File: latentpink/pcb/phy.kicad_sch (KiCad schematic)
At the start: 0 parts

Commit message: Continued initial schematic capture and floorplanning
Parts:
- added U1: VSC8512, azonenberg_pcb:BGA_672_27x27_DEPOPCORNER_1MM, symbol microchip-azonenberg:VSC8512
- added U2: XC7K160T-2FBG484C, azonenberg_pcb:BGA_484_22x22_FULLARRAY_1MM, symbol xilinx-azonenberg:XC7KxT-FBG484
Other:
- added sheet QSGMII Power (qsgmii-power.kicad_sch)
- company: (none) -> Antikernel Labs

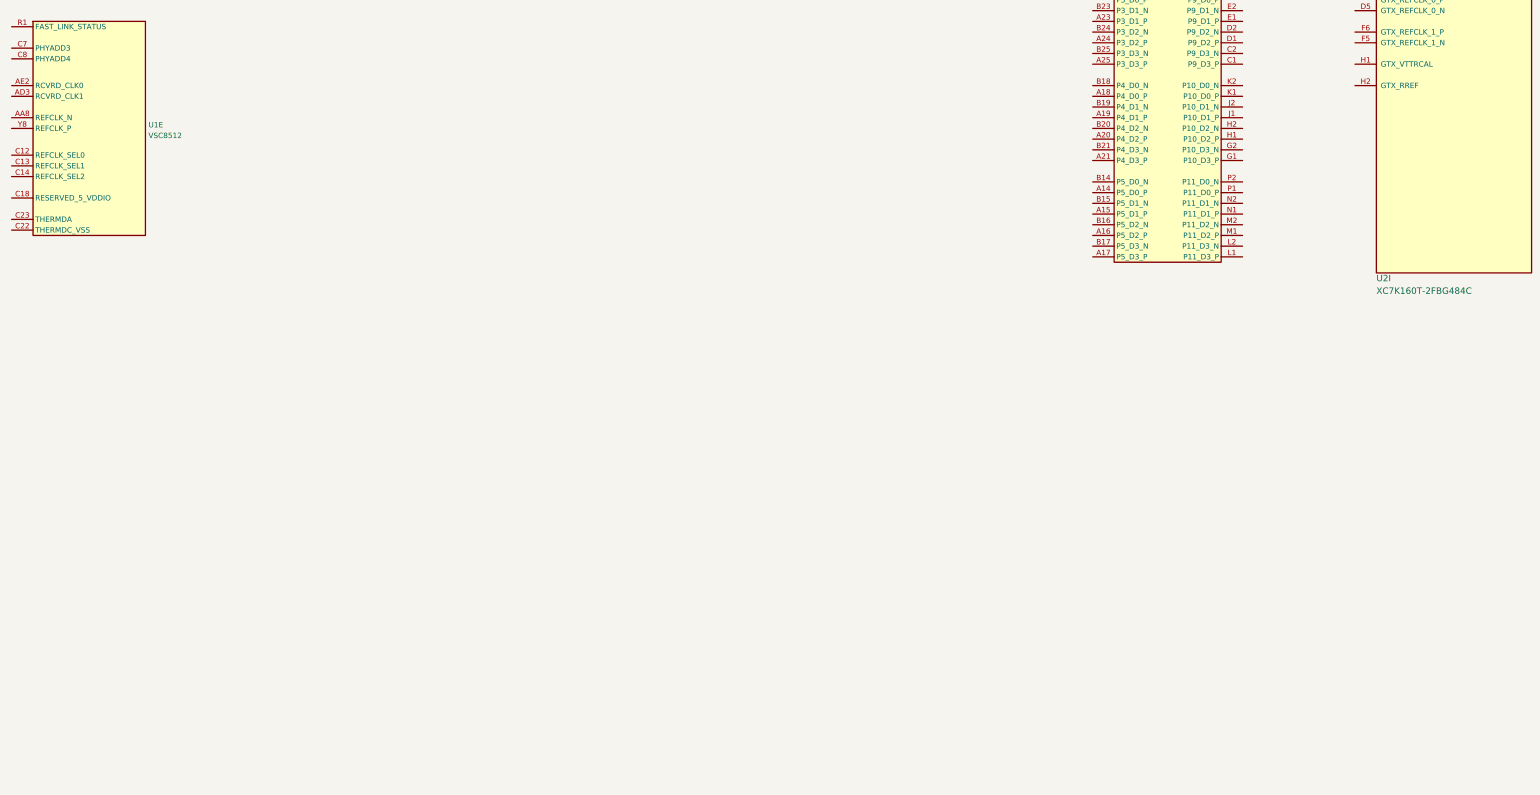
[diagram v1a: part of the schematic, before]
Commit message: Continued initial schematic capture
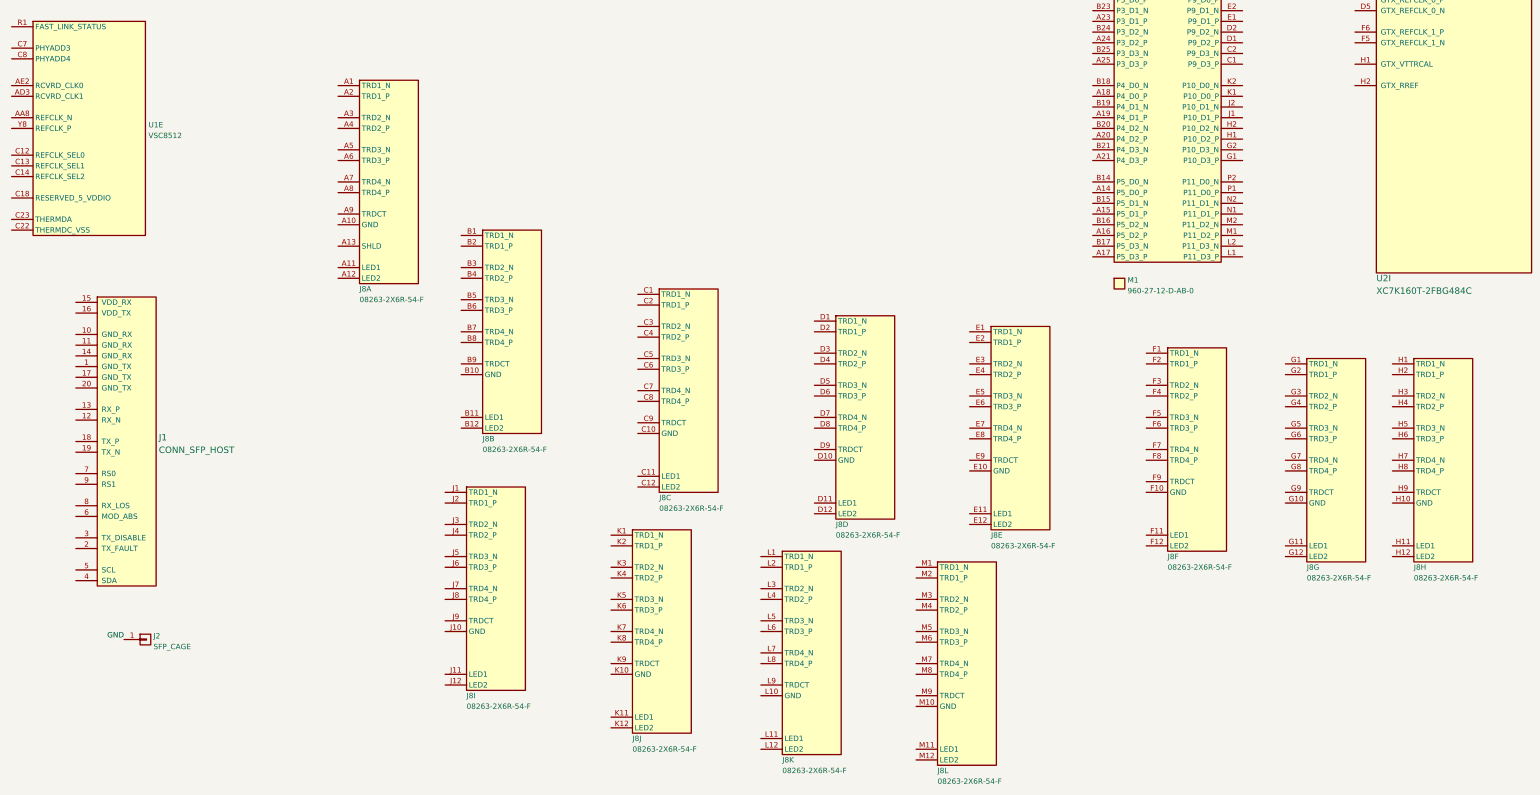
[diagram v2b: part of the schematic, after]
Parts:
- added J1: CONN_SFP_HOST, azonenberg_pcb:CONN_SFP+_AMPHENOL_UE76_A10_2000T, symbol special-azonenberg:CONN_SFP_HOST
- added J2: SFP_CAGE, azonenberg_pcb:CONN_SFP_CAGE_TE_2007194-1, symbol conn:CONN_01X01
- added J8: 08263-2X6R-54-F, azonenberg_pcb:CONN_RJ45_BELFUSE_0863-2X6R-54-F, symbol special-azonenberg:BEL_FUSE_08263-2X6R-54-F
- added M1: 960-27-12-D-AB-0, azonenberg_pcb:HEATSINK_WAKEFIELDVETTE_960-27-12-D-AB-0, symbol special-azonenberg:MECHANICAL
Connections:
- new net GND: J2.1 (P1)

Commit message: Continued work on QSGMII subsystem
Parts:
- added C334, C335, C336, C337, C338, C339, C340, C341, C342, C343, C346, C347, C348, C349, C350, C351: 0.1 uF, azonenberg_pcb:EIA_0402_CAP_NOSILK, symbol device:C
- added C344, C345: 0.47 uF, azonenberg_pcb:EIA_0402_CAP_NOSILK, symbol device:C
- added R78, R79: 4.7K, azonenberg_pcb:EIA_0402_RES_NOSILK, symbol device:R
- added R80: 100, symbol device:R
- added U24, U25: OSC_LVDS, symbol osc-azonenberg:OSC_LVDS
- added U4: STM32H735-UFBGA176-25, azonenberg_pcb:BGA_201_10x10_DEPOP_0.65MM_OSHPARK, symbol st-azonenberg:STM32H735-UFBGA176-25
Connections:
- net GND: now also J1.1 (GND_TX), J1.10 (GND_RX), J1.11 (GND_RX), J1.14 (GND_RX), J1.17 (GND_TX), J1.20 (GND_TX), J8.A10 (GND), J8.B10 (GND), J8.C10 (GND), J8.D10 (GND), J8.E10 (GND), J8.F10 (GND), J8.G10 (GND), J8.H10 (GND), J8.J10 (GND), J8.K10 (GND), J8.L10 (GND), J8.M10 (GND)
- net ETH6_D0_P: now reaches U1.A10 (P6_D0_P)
- net ETH6_D0_P: now also J8.G2 (TRD1_P)
- net ETH6_D1_P: now reaches U1.A11 (P6_D1_P)
- net ETH6_D1_P: now also J8.G4 (TRD2_P)
- net ETH6_D2_P: now reaches U1.A12 (P6_D2_P)
- net ETH6_D2_P: now also J8.G6 (TRD3_P)
- net ETH6_D3_P: now reaches U1.A13 (P6_D3_P)
- net ETH6_D3_P: now also J8.G8 (TRD4_P)
- net ETH5_D0_P: now reaches U1.A14 (P5_D0_P)
- net ETH5_D0_P: now also J8.F2 (TRD1_P)
- net ETH5_D1_P: now reaches U1.A15 (P5_D1_P)
- net ETH5_D1_P: now also J8.F4 (TRD2_P)
- net ETH5_D2_P: now reaches U1.A16 (P5_D2_P)
- net ETH5_D2_P: now also J8.F6 (TRD3_P)
- net ETH5_D3_P: now reaches U1.A17 (P5_D3_P)
- net ETH5_D3_P: now also J8.F8 (TRD4_P)
- net ETH4_D0_P: now reaches U1.A18 (P4_D0_P)
- net ETH4_D0_P: now also J8.E2 (TRD1_P)
- net ETH4_D1_P: now reaches U1.A19 (P4_D1_P)
- net ETH4_D1_P: now also J8.E4 (TRD2_P)
- net ETH8_D0_P: now reaches U1.A2 (P8_D0_P)
- net ETH8_D0_P: now also J8.J2 (TRD1_P)
- net ETH4_D2_P: now reaches U1.A20 (P4_D2_P)
- net ETH4_D2_P: now also J8.E6 (TRD3_P)
- net ETH4_D3_P: now reaches U1.A21 (P4_D3_P)
- net ETH4_D3_P: now also J8.E8 (TRD4_P)
- net ETH3_D0_P: now reaches U1.A22 (P3_D0_P)
- net ETH3_D0_P: now also J8.D2 (TRD1_P)
- net ETH3_D1_P: now reaches U1.A23 (P3_D1_P)
- net ETH3_D1_P: now also J8.D4 (TRD2_P)
- net ETH3_D2_P: now reaches U1.A24 (P3_D2_P)
- net ETH3_D2_P: now also J8.D6 (TRD3_P)
- net ETH3_D3_P: now reaches U1.A25 (P3_D3_P)
- net ETH3_D3_P: now also J8.D8 (TRD4_P)
- net ETH8_D1_P: now reaches U1.A3 (P8_D1_P)
- net ETH8_D1_P: now also J8.J4 (TRD2_P)
- net ETH8_D2_P: now reaches U1.A4 (P8_D2_P)
- net ETH8_D2_P: now also J8.J6 (TRD3_P)
- net ETH8_D3_P: now reaches U1.A5 (P8_D3_P)
- net ETH8_D3_P: now also J8.J8 (TRD4_P)
- net ETH7_D0_P: now reaches U1.A6 (P7_D0_P)
- net ETH7_D0_P: now also J8.H2 (TRD1_P)
- net ETH7_D1_P: now reaches U1.A7 (P7_D1_P)
- net ETH7_D1_P: now also J8.H4 (TRD2_P)
- net ETH7_D2_P: now reaches U1.A8 (P7_D2_P)
- net ETH7_D2_P: now also J8.H6 (TRD3_P)
- net ETH7_D3_P: now reaches U1.A9 (P7_D3_P)
- net ETH7_D3_P: now also J8.H8 (TRD4_P)
- net ETH6_D0_N: now reaches U1.B10 (P6_D0_N)
- net ETH6_D0_N: now also J8.G1 (TRD1_N)
- net ETH6_D1_N: now reaches U1.B11 (P6_D1_N)
- net ETH6_D1_N: now also J8.G3 (TRD2_N)
- net ETH6_D2_N: now reaches U1.B12 (P6_D2_N)
- net ETH6_D2_N: now also J8.G5 (TRD3_N)
- net ETH6_D3_N: now reaches U1.B13 (P6_D3_N)
- net ETH6_D3_N: now also J8.G7 (TRD4_N)
- net ETH5_D0_N: now reaches U1.B14 (P5_D0_N)
- net ETH5_D0_N: now also J8.F1 (TRD1_N)
- net ETH5_D1_N: now reaches U1.B15 (P5_D1_N)
- net ETH5_D1_N: now also J8.F3 (TRD2_N)
- net ETH5_D2_N: now reaches U1.B16 (P5_D2_N)
- net ETH5_D2_N: now also J8.F5 (TRD3_N)
- net ETH5_D3_N: now reaches U1.B17 (P5_D3_N)
- net ETH5_D3_N: now also J8.F7 (TRD4_N)
- net ETH4_D0_N: now reaches U1.B18 (P4_D0_N)
- net ETH4_D0_N: now also J8.E1 (TRD1_N)
- net ETH4_D1_N: now reaches U1.B19 (P4_D1_N)
- net ETH4_D1_N: now also J8.E3 (TRD2_N)
- net ETH8_D0_N: now reaches U1.B2 (P8_D0_N)
- net ETH8_D0_N: now also J8.J1 (TRD1_N)
- net ETH4_D2_N: now reaches U1.B20 (P4_D2_N)
- net ETH4_D2_N: now also J8.E5 (TRD3_N)
- net ETH4_D3_N: now reaches U1.B21 (P4_D3_N)
- net ETH4_D3_N: now also J8.E7 (TRD4_N)
- net ETH3_D0_N: now reaches U1.B22 (P3_D0_N)
- net ETH3_D0_N: now also J8.D1 (TRD1_N)
- net ETH3_D1_N: now reaches U1.B23 (P3_D1_N)
- net ETH3_D1_N: now also J8.D3 (TRD2_N)
- net ETH3_D2_N: now reaches U1.B24 (P3_D2_N)
- net ETH3_D2_N: now also J8.D5 (TRD3_N)
- net ETH3_D3_N: now reaches U1.B25 (P3_D3_N)
- net ETH3_D3_N: now also J8.D7 (TRD4_N)
- net ETH8_D1_N: now reaches U1.B3 (P8_D1_N)
- net ETH8_D1_N: now also J8.J3 (TRD2_N)
- net ETH8_D2_N: now reaches U1.B4 (B8_D2_N)
- net ETH8_D2_N: now also J8.J5 (TRD3_N)
- net ETH8_D3_N: now reaches U1.B5 (P8_D3_N)
- net ETH8_D3_N: now also J8.J7 (TRD4_N)
- net ETH7_D0_N: now reaches U1.B6 (P7_D0_N)
- net ETH7_D0_N: now also J8.H1 (TRD1_N)
- net ETH7_D1_N: now reaches U1.B7 (P7_D1_N)
- net ETH7_D1_N: now also J8.H3 (TRD2_N)
- net ETH7_D2_N: now reaches U1.B8 (B7_D2_N)
- net ETH7_D2_N: now also J8.H5 (TRD3_N)
- net ETH7_D3_N: now reaches U1.B9 (P7_D3_N)
- net ETH7_D3_N: now also J8.H7 (TRD4_N)
- net ETH9_D3_P: now reaches U1.C1 (P9_D3_P)
- net ETH9_D3_P: now also J8.K8 (TRD4_P)
- net ETH9_D3_N: now reaches U1.C2 (P9_D3_N)
- net ETH9_D3_N: now also J8.K7 (TRD4_N)
- net ETH2_D0_N: now reaches U1.C25 (P2_D0_N)
- net ETH2_D0_N: now also J8.C1 (TRD1_N)
- net ETH2_D0_P: now reaches U1.C26 (P2_D0_P)
- net ETH2_D0_P: now also J8.C2 (TRD1_P)
- net ETH9_D2_P: now reaches U1.D1 (P9_D2_P)
- net ETH9_D2_P: now also J8.K6 (TRD3_P)
- net ETH9_D2_N: now reaches U1.D2 (P9_D2_N)
- net ETH9_D2_N: now also J8.K5 (TRD3_N)
- net ETH2_D1_N: now reaches U1.D25 (P2_D1_N)
- net ETH2_D1_N: now also J8.C3 (TRD2_N)
- net ETH2_D1_P: now reaches U1.D26 (P2_D1_P)
- net ETH2_D1_P: now also J8.C4 (TRD2_P)
- net ETH9_D1_P: now reaches U1.E1 (P9_D1_P)
- net ETH9_D1_P: now also J8.K4 (TRD2_P)
- net ETH9_D1_N: now reaches U1.E2 (P9_D1_N)
- net ETH9_D1_N: now also J8.K3 (TRD2_N)
- net ETH2_D2_N: now reaches U1.E25 (P2_D2_N)
- net ETH2_D2_N: now also J8.C5 (TRD3_N)
- net ETH2_D2_P: now reaches U1.E26 (P2_D2_P)
- net ETH2_D2_P: now also J8.C6 (TRD3_P)
- net ETH9_D0_P: now reaches U1.F1 (P9_D0_P)
- net ETH9_D0_P: now also J8.K2 (TRD1_P)
- net ETH9_D0_N: now reaches U1.F2 (P9_D0_N)
- net ETH9_D0_N: now also J8.K1 (TRD1_N)
- net ETH2_D3_N: now reaches U1.F25 (P2_D3_N)
- net ETH2_D3_N: now also J8.C7 (TRD4_N)
- net ETH2_D3_P: now reaches U1.F26 (P2_D3_P)
- net ETH2_D3_P: now also J8.C8 (TRD4_P)
- net ETH10_D3_P: now reaches U1.G1 (P10_D3_P)
- net ETH10_D3_P: now also J8.L8 (TRD4_P)
- net ETH10_D3_N: now reaches U1.G2 (P10_D3_N)
- net ETH10_D3_N: now also J8.L7 (TRD4_N)
- net ETH1_D0_N: now reaches U1.G25 (P1_D0_N)
- net ETH1_D0_N: now also J8.B1 (TRD1_N)
- net ETH1_D0_P: now reaches U1.G26 (P1_D0_P)
- net ETH1_D0_P: now also J8.B2 (TRD1_P)
- net ETH10_D2_P: now reaches U1.H1 (P10_D2_P)
- net ETH10_D2_P: now also J8.L6 (TRD3_P)
- net ETH10_D2_N: now reaches U1.H2 (P10_D2_N)
- net ETH10_D2_N: now also J8.L5 (TRD3_N)
- net ETH1_D1_N: now reaches U1.H25 (P1_D1_N)
- net ETH1_D1_N: now also J8.B3 (TRD2_N)
- net ETH1_D1_P: now reaches U1.H26 (P1_D1_P)
- net ETH1_D1_P: now also J8.B4 (TRD2_P)
- net ETH10_D1_P: now reaches U1.J1 (P10_D1_P)
- net ETH10_D1_P: now also J8.L4 (TRD2_P)
- net ETH10_D1_N: now reaches U1.J2 (P10_D1_N)
- net ETH10_D1_N: now also J8.L3 (TRD2_N)
- net ETH1_D2_N: now reaches U1.J25 (P1_D2_N)
- net ETH1_D2_N: now also J8.B5 (TRD3_N)
- net ETH1_D2_P: now reaches U1.J26 (P1_D2_P)
- net ETH1_D2_P: now also J8.B6 (TRD3_P)
- net ETH10_D0_P: now reaches U1.K1 (P10_D0_P)
- net ETH10_D0_P: now also J8.L2 (TRD1_P)
- net ETH10_D0_N: now reaches U1.K2 (P10_D0_N)
- net ETH10_D0_N: now also J8.L1 (TRD1_N)
- net ETH1_D3_N: now reaches U1.K25 (P1_D3_N)
- net ETH1_D3_N: now also J8.B7 (TRD4_N)
- net ETH1_D3_P: now reaches U1.K26 (P1_D3_P)
- net ETH1_D3_P: now also J8.B8 (TRD4_P)
- net ETH11_D3_P: now reaches U1.L1 (P11_D3_P)
- net ETH11_D3_P: now also J8.M8 (TRD4_P)
- net ETH11_D3_N: now reaches U1.L2 (P11_D3_N)
- net ETH11_D3_N: now also J8.M7 (TRD4_N)
- net ETH0_D0_N: now reaches U1.L25 (P0_D0_N)
- net ETH0_D0_N: now also J8.A1 (TRD1_N)
- net ETH0_D0_P: now reaches U1.L26 (P0_D0_P)
- net ETH0_D0_P: now also J8.A2 (TRD1_P)
- net ETH11_D2_P: now reaches U1.M1 (P11_D2_P)
- net ETH11_D2_P: now also J8.M6 (TRD3_P)
- net ETH11_D2_N: now reaches U1.M2 (P11_D2_N)
- net ETH11_D2_N: now also J8.M5 (TRD3_N)
- net ETH0_D1_N: now reaches U1.M25 (P0_D1_N)
- net ETH0_D1_N: now also J8.A3 (TRD2_N)
- net ETH0_D1_P: now reaches U1.M26 (P0_D1_P)
- net ETH0_D1_P: now also J8.A4 (TRD2_P)
- net ETH11_D1_P: now reaches U1.N1 (P11_D1_P)
- net ETH11_D1_P: now also J8.M4 (TRD2_P)
- net ETH11_D1_N: now reaches U1.N2 (P11_D1_N)
- net ETH11_D1_N: now also J8.M3 (TRD2_N)
- net ETH0_D2_N: now reaches U1.N25 (P0_D2_N)
- net ETH0_D2_N: now also J8.A5 (TRD3_N)
- net ETH0_D2_P: now reaches U1.N26 (P0_D2_P)
- net ETH0_D2_P: now also J8.A6 (TRD3_P)
- net ETH11_D0_P: now reaches U1.P1 (P11_D0_P)
- net ETH11_D0_P: now also J8.M2 (TRD1_P)
- net ETH11_D0_N: now reaches U1.P2 (P11_D0_N)
- net ETH11_D0_N: now also J8.M1 (TRD1_N)
- net ETH0_D3_N: now reaches U1.P25 (P0_D3_N)
- net ETH0_D3_N: now also J8.A7 (TRD4_N)
- net ETH0_D3_P: now reaches U1.P26 (P0_D3_P)
- net ETH0_D3_P: now also J8.A8 (TRD4_P)
- net SFP_TX_N: now reaches U2.A3 (GTX_TX_3_N)
- net SFP_TX_N: now also J1.19 (TX_N)
- net SFP_TX_P: now reaches U2.A4 (GTX_TX_3_P)
- net SFP_TX_P: now also J1.18 (TX_P)
- net QSGMII_0_TX_N: now reaches U2.B1 (GTX_TX_2_N)
- net QSGMII_0_TX_N: now also C335.1
- net QSGMII_0_TX_P: now reaches U2.B2 (GTX_TX_2_P)
- net QSGMII_0_TX_P: now also C334.1
- net SFP_RX_N: now reaches U2.B5 (GTX_RX_3_N)
- net SFP_RX_N: now also J1.12 (RX_N)
- net SFP_RX_P: now reaches U2.B6 (GTX_RX_3_P)
- net SFP_RX_P: now also J1.13 (RX_P)
- net QSGMII_0_RX_N: now reaches U2.C3 (GTX_RX_2_N)
- net QSGMII_0_RX_N: now also C337.1
- net QSGMII_0_RX_P: now reaches U2.C4 (GTX_RX_2_P)
- net QSGMII_0_RX_P: now also C336.1
- net QSGMII_1_TX_N: now reaches U2.D1 (GTX_TX_1_N)
- net QSGMII_1_TX_N: now also C339.1
- net QSGMII_1_TX_P: now reaches U2.D2 (GTX_TX_1_P)
- net QSGMII_1_TX_P: now also C338.1
- net GTX_REFCLK_156M25_N: now reaches U2.D5 (GTX_REFCLK_0_N)
- net GTX_REFCLK_156M25_P: now reaches U2.D6 (GTX_REFCLK_0_P)
- net QSGMII_1_RX_N: now reaches U2.E3 (GTX_RX_1_N)
- net QSGMII_1_RX_N: now also C347.1
- net QSGMII_1_RX_P: now reaches U2.E4 (GTX_RX_1_P)
- net QSGMII_1_RX_P: now also C346.1
- net QSGMII_2_TX_N: now reaches U2.F1 (GTX_TX_0_N)
- net QSGMII_2_TX_N: now also C349.1
- net QSGMII_2_TX_P: now reaches U2.F2 (GTX_TX_0_P)
- net QSGMII_2_TX_P: now also C348.1
- net GTX_REFCLK_SPARE_N: now reaches U2.F5 (GTX_REFCLK_1_N)
- net GTX_REFCLK_SPARE_P: now reaches U2.F6 (GTX_REFCLK_1_P)
- net QSGMII_2_RX_N: now reaches U2.G3 (GTX_RX_0_N)
- net QSGMII_2_RX_N: now also C351.1
- net QSGMII_2_RX_P: now reaches U2.G4 (GTX_RX_0_P)
- net QSGMII_2_RX_P: now also C350.1
- net at U2.H1 (GTX_VTTRCAL): now also R80.2
- net at U2.H2 (GTX_RREF): now also R80.1
- net SFP_VDD_RX: now reaches J1.15 (VDD_RX)
- net SFP_VDD_TX: now reaches J1.16 (VDD_TX)
- net SFP_TX_FAULT: now reaches J1.2 (TX_FAULT)
- net SFP_TX_FAULT: now also U4.M11 (PH7)
- net SFP_TX_DISABLE: now reaches J1.3 (TX_DISABLE)
- net SFP_TX_DISABLE: now also U4.P15 (PH6)
- net SFP_I2C_SDA: now reaches J1.4 (SDA)
- net SFP_I2C_SDA: now also R78.1, U4.R5 (PH5)
- net SFP_I2C_SCL: now reaches J1.5 (SCL)
- net SFP_I2C_SCL: now also R79.1, U4.P4 (PH4)
- net SFP_MOD_ABS: now reaches J1.6 (MOD_ABS)
- net SFP_MOD_ABS: now also U4.R4 (PH3)
- net SFP_RS0: now reaches J1.7 (RS0)
- net SFP_RS0: now also U4.J1 (PH0)
- net SFP_RX_LOS: now reaches J1.8 (RX_LOS)
- net SFP_RX_LOS: now also U4.N4 (PH2)
- net SFP_RS1: now reaches J1.9 (RS1)
- net SFP_RS1: now also U4.K1 (PH1)
- net QSGMII_1_RX_AC_N: now reaches U1.AA13 (SERDES_E2_TX_N)
- net QSGMII_1_RX_AC_N: now also C347.2
- net QSGMII_0_RX_AC_N: now reaches U1.AA17 (SERDES_E1_TX_N)
- net QSGMII_0_RX_AC_N: now also C337.2
- net QSGMII_2_RX_AC_N: now reaches U1.AA9 (SERDES_E3_TX_N)
- net QSGMII_2_RX_AC_N: now also C351.2
- net QSGMII_1_TX_AC_P: now reaches U1.AE13 (SERDES_E2_RX_P)
- net QSGMII_1_TX_AC_P: now also C338.2
- net QSGMII_0_TX_AC_P: now reaches U1.AE17 (SERDES_E1_RX_P)
- net QSGMII_0_TX_AC_P: now also C334.2
- net QSGMII_2_TX_AC_P: now reaches U1.AE9 (SERDES_E3_RX_P)
- net QSGMII_2_TX_AC_P: now also C348.2
- net QSGMII_1_TX_AC_N: now reaches U1.AF13 (SERDES_E2_RX_N)
- net QSGMII_1_TX_AC_N: now also C339.2
- net QSGMII_0_TX_AC_N: now reaches U1.AF17 (SERDES_E1_RX_N)
- net QSGMII_0_TX_AC_N: now also C335.2
- net QSGMII_2_TX_AC_N: now reaches U1.AF9 (SERDES_E3_RX_N)
- net QSGMII_2_TX_AC_N: now also C349.2
- net QSGMII_1_RX_AC_P: now reaches U1.Y13 (SERDES_E2_TX_P)
- net QSGMII_1_RX_AC_P: now also C346.2
- net QSGMII_0_RX_AC_P: now reaches U1.Y17 (SERDES_E1_TX_P)
- net QSGMII_0_RX_AC_P: now also C336.2
- net QSGMII_2_RX_AC_P: now reaches U1.Y9 (SERDES_E3_TX_P)
- net QSGMII_2_RX_AC_P: now also C350.2
- new net 3V3: R78.2, R79.2
- no-connect marks 0 -> 44
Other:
- sheet QSGMII Power ports: added 1V0, 2V5, GND; removed none
- note added: "One LED per RJ45 (bi color) but VSC8512 has two single LED pins"
- note added: "TODO: SFP power"
- note added: "TODO: refclks Can use 156.25 for both, provide a second DNP oscillator just in case"
- moved on the sheet: J1, J2, J8A, J8B, J8C, J8D, J8E, J8F, J8G, J8H, J8I, J8J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

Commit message: Switched to new RJ45 for LATENTPINK, continued general PHY schematic
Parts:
- removed J8: 08263-2X6R-54-F, azonenberg_pcb:CONN_RJ45_BELFUSE_0863-2X6R-54-F, symbol special-azonenberg:BEL_FUSE_08263-2X6R-54-F
- added C352, C353, C354: 1 uF, symbol device:C
- added J18, J19, J20, J21, J4, J8: BEL_FUSE_0845-2R1T-E4, azonenberg_pcb:CONN_RJ45_BELFUSE_0845-2R1T-E4, symbol special-azonenberg:BEL_FUSE_0845-2R1T-E4
- added J3: XILINX_JTAG, azonenberg_pcb:XILINX_JTAG_PTH_MOLEX_0878311420, symbol xilinx-azonenberg:XILINX_JTAG
- added R100, R101, R102, R103, R104, R81, R82, R83, R84, R85, R86, R87, R88, R89, R90, R91, R92, R93, R94, R95, R96, R97, R98, R99: 470, azonenberg_pcb:EIA_0402_RES_NOSILK, symbol device:R
- added R105: 620 1%, symbol device:R
- added R106, R107: 1K, azonenberg_pcb:EIA_0402_RES_NOSILK, symbol device:R
- added R108: 1K, symbol device:R
- added R109, R110, R111: 2K 1%, symbol device:R
- added TP19, TP20: TESTPOINT, symbol conn:CONN_01X01
- R80: footprint (none) -> azonenberg_pcb:EIA_0402_RES_NOSILK
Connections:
- net 2V5: now also U1.C18 (RESERVED_5_VDDIO), J3.2 (Vccaux), R106.2, R107.2, R108.1
- net 3V3: now also J18.28 (LED1_P), J18.30 (LED2_G_P), J18.32 (LED1_P), J18.34 (LED2_G_P), J19.28 (LED1_P), J19.30 (LED2_G_P), J19.32 (LED1_P), J19.34 (LED2_G_P), J20.28 (LED1_P), J20.30 (LED2_G_P), J20.32 (LED1_P), J20.34 (LED2_G_P), J21.28 (LED1_P), J21.30 (LED2_G_P), J21.32 (LED1_P), J21.34 (LED2_G_P), J4.28 (LED1_P), J4.30 (LED2_G_P), J4.32 (LED1_P), J4.34 (LED2_G_P), J8.28 (LED1_P), J8.30 (LED2_G_P), J8.32 (LED1_P), J8.34 (LED2_G_P)
- net ETH0_D0_N: now also J4.13 (BI_DA_N)
- net ETH0_D0_P: now also J4.6 (BI_DA_P)
- net ETH0_D1_N: now also J4.5 (BI_DB_N)
- net ETH0_D1_P: now also J4.11 (BI_DB_P)
- net ETH0_D2_N: now also J4.10 (BI_DC_N)
- net ETH0_D2_P: now also J4.3 (BI_DC_P)
- net ETH0_D3_N: now also J4.2 (BI_DD_N)
- net ETH0_D3_P: now also J4.9 (BI_DD_P)
- net ETH10_D0_N: now also J21.13 (BI_DA_N)
- net ETH10_D0_P: now also J21.6 (BI_DA_P)
- net ETH10_D1_N: now also J21.5 (BI_DB_N)
- net ETH10_D1_P: now also J21.11 (BI_DB_P)
- net ETH10_D2_N: now also J21.10 (BI_DC_N)
- net ETH10_D2_P: now also J21.3 (BI_DC_P)
- net ETH10_D3_N: now also J21.2 (BI_DD_N)
- net ETH10_D3_P: now also J21.9 (BI_DD_P)
- net ETH11_D0_N: now also J21.21 (BI_DA_N)
- net ETH11_D0_P: now also J21.15 (BI_DA_P)
- net ETH11_D1_N: now also J21.16 (BI_DB_N)
- net ETH11_D1_P: now also J21.23 (BI_DB_P)
- net ETH11_D2_N: now also J21.24 (BI_DC_N)
- net ETH11_D2_P: now also J21.18 (BI_DC_P)
- net ETH11_D3_N: now also J21.19 (BI_DD_N)
- net ETH11_D3_P: now also J21.26 (BI_DD_P)
- net ETH1_D0_N: now also J4.21 (BI_DA_N)
- net ETH1_D0_P: now also J4.15 (BI_DA_P)
- net ETH1_D1_N: now also J4.16 (BI_DB_N)
- net ETH1_D1_P: now also J4.23 (BI_DB_P)
- net ETH1_D2_N: now also J4.24 (BI_DC_N)
- net ETH1_D2_P: now also J4.18 (BI_DC_P)
- net ETH1_D3_N: now also J4.19 (BI_DD_N)
- net ETH1_D3_P: now also J4.26 (BI_DD_P)
- net ETH2_D0_N: now also J8.13 (BI_DA_N)
- net ETH2_D0_P: now also J8.6 (BI_DA_P)
- net ETH2_D1_N: now also J8.5 (BI_DB_N)
- net ETH2_D1_P: now also J8.11 (BI_DB_P)
- net ETH2_D2_N: now also J8.10 (BI_DC_N)
- net ETH2_D2_P: now also J8.3 (BI_DC_P)
- net ETH2_D3_N: now also J8.2 (BI_DD_N)
- net ETH2_D3_P: now also J8.9 (BI_DD_P)
- net ETH3_D0_N: now also J8.21 (BI_DA_N)
- net ETH3_D0_P: now also J8.15 (BI_DA_P)
- net ETH3_D1_N: now also J8.16 (BI_DB_N)
- net ETH3_D1_P: now also J8.23 (BI_DB_P)
- net ETH3_D2_N: now also J8.24 (BI_DC_N)
- net ETH3_D2_P: now also J8.18 (BI_DC_P)
- net ETH3_D3_N: now also J8.19 (BI_DD_N)
- net ETH3_D3_P: now also J8.26 (BI_DD_P)
- net ETH4_D0_N: now also J18.13 (BI_DA_N)
- net ETH4_D0_P: now also J18.6 (BI_DA_P)
- net ETH4_D1_N: now also J18.5 (BI_DB_N)
- net ETH4_D1_P: now also J18.11 (BI_DB_P)
- net ETH4_D2_N: now also J18.10 (BI_DC_N)
- net ETH4_D2_P: now also J18.3 (BI_DC_P)
- net ETH4_D3_N: now also J18.2 (BI_DD_N)
- net ETH4_D3_P: now also J18.9 (BI_DD_P)
- net ETH5_D0_N: now also J18.21 (BI_DA_N)
- net ETH5_D0_P: now also J18.15 (BI_DA_P)
- net ETH5_D1_N: now also J18.16 (BI_DB_N)
- net ETH5_D1_P: now also J18.23 (BI_DB_P)
- net ETH5_D2_N: now also J18.24 (BI_DC_N)
- net ETH5_D2_P: now also J18.18 (BI_DC_P)
- net ETH5_D3_N: now also J18.19 (BI_DD_N)
- net ETH5_D3_P: now also J18.26 (BI_DD_P)
- net ETH6_D0_N: now also J19.13 (BI_DA_N)
- net ETH6_D0_P: now also J19.6 (BI_DA_P)
- net ETH6_D1_N: now also J19.5 (BI_DB_N)
- net ETH6_D1_P: now also J19.11 (BI_DB_P)
- net ETH6_D2_N: now also J19.10 (BI_DC_N)
- net ETH6_D2_P: now also J19.3 (BI_DC_P)
- net ETH6_D3_N: now also J19.2 (BI_DD_N)
- net ETH6_D3_P: now also J19.9 (BI_DD_P)
- net ETH7_D0_N: now also J19.21 (BI_DA_N)
- net ETH7_D0_P: now also J19.15 (BI_DA_P)
- net ETH7_D1_N: now also J19.16 (BI_DB_N)
- net ETH7_D1_P: now also J19.23 (BI_DB_P)
- net ETH7_D2_N: now also J19.24 (BI_DC_N)
- net ETH7_D2_P: now also J19.18 (BI_DC_P)
- net ETH7_D3_N: now also J19.19 (BI_DD_N)
- net ETH7_D3_P: now also J19.26 (BI_DD_P)
- net ETH8_D0_N: now also J20.13 (BI_DA_N)
- net ETH8_D0_P: now also J20.6 (BI_DA_P)
- net ETH8_D1_N: now also J20.5 (BI_DB_N)
- net ETH8_D1_P: now also J20.11 (BI_DB_P)
- net ETH8_D2_N: now also J20.10 (BI_DC_N)
- net ETH8_D2_P: now also J20.3 (BI_DC_P)
- net ETH8_D3_N: now also J20.2 (BI_DD_N)
- net ETH8_D3_P: now also J20.9 (BI_DD_P)
- net ETH9_D0_N: now also J20.21 (BI_DA_N)
- net ETH9_D0_P: now also J20.15 (BI_DA_P)
- net ETH9_D1_N: now also J20.16 (BI_DB_N)
- net ETH9_D1_P: now also J20.23 (BI_DB_P)
- net ETH9_D2_N: now also J20.24 (BI_DC_N)
- net ETH9_D2_P: now also J20.18 (BI_DC_P)
- net ETH9_D3_N: now also J20.19 (BI_DD_N)
- net ETH9_D3_P: now also J20.26 (BI_DD_P)
- net GND: now also U1.C12 (REFCLK_SEL0), U1.C13 (REFCLK_SEL1), U1.C14 (REFCLK_SEL2), U1.C22 (THERMDC_VSS), U1.C23 (THERMDA), U1.C7 (PHYADD3), U1.C8 (PHYADD4), C352.2, C353.2, C354.2, J18.1 (GND), J18.20 (GND), J19.1 (GND), J19.20 (GND), J20.1 (GND), J20.20 (GND), J21.1 (GND), J21.20 (GND), J3.11 (Vss), J3.3 (Vss), J3.5 (Vss), J3.7 (Vss), J3.9 (Vss), J4.1 (GND), J4.20 (GND), J8.1 (GND), J8.20 (GND), R109.1, R110.1, R111.1
- net VSC_CLKOUT_1: now reaches U1.AD3 (RCVRD_CLK1)
- net VSC_CLKOUT_1: now also TP19.1 (P1)
- net VSC_CLKOUT_0: now reaches U1.AE2 (RCVRD_CLK0)
- net VSC_CLKOUT_0: now also TP20.1 (P1)
- net VSC_FAST_STATUS: now reaches U1.R1 (FAST_LINK_STATUS)
- net VSC_POWERDOWN: now reaches U4.B12 (PH14)
- net VSC_POWERDOWN: now also U1.C3 (COMA_MODE), R107.1
- net VSC_RST_N: now reaches U4.D12 (PH15)
- net VSC_RST_N: now also U1.C4 (RST#), R106.1
- net at U1.AA1 (PHY2_LED1): now also R95.2
- net at U1.AA2 (PHY1_LED1): now also R94.2
- net at U1.AA3 (PHY0_LED1): now also R93.2
- net at U1.R4 (PHY11_LED0): now also R92.2
- net at U1.T1 (PHY10_LED0): now also R91.2
- net at U1.T2 (PHY9_LED0): now also R90.2
- net at U1.T3 (PHY8_LED0): now also R89.2
- net at U1.T4 (PHY7_LED0): now also R88.2
- net at U1.U1 (PHY6_LED0): now also R87.2
- net at U1.U2 (PHY5_LED0): now also R86.2
- net at U1.U3 (PHY4_LED0): now also R85.2
- net at U1.U4 (PHY3_LED0): now also R84.2
- net at U1.V1 (PHY2_LED0): now also R83.2
- net at U1.V2 (PHY1_LED0): now also R82.2
- net at U1.V3 (PHY0_LED0): now also R81.2
- net at U1.V4 (PHY11_LED1): now also R104.2
- net at U1.W1 (PHY10_LED1): now also R103.2
- net at U1.W2 (PHY9_LED1): now also R102.2
- net at U1.W3 (PHY8_LED1): now also R101.2
- net at U1.W4 (PHY7_LED1): now also R100.2
- net at U1.Y1 (PHY6_LED1): now also R99.2
- net at U1.Y2 (PHY5_LED1): now also R98.2
- net at U1.Y3 (PHY4_LED1): now also R97.2
- net at U1.Y4 (PHY3_LED1): now also R96.2
- net at U1.AE22 (SERDES_REXT0): now also R105.1
- net at U1.AF22 (SERDES_REXT1): now also R105.2
- net VSC_MDIO: now reaches U1.AF3 (MDIO)
- net VSC_MDC: now reaches U1.AF4 (MDC)
- net VSC_JTAG_TCK: now reaches U1.D17 (JTAG_TCK)
- net VSC_JTAG_TCK: now also J3.6 (TCK)
- net VSC_JTAG_TDI: now reaches U1.D18 (JTAG_TDI)
- net VSC_JTAG_TDI: now also J3.10 (TDI_OUT)
- net VSC_JTAG_TDO: now reaches U1.D19 (JTAG_TDO)
- net VSC_JTAG_TDO: now also J3.8 (TDO_IN)
- net VSC_JTAG_TMS: now reaches U1.D20 (JTAG_TMS)
- net VSC_JTAG_TMS: now also J3.4 (TMS)
- net at U1.D21 (JTAG_TRST): now also R108.2
- net at U1.E13 (REF_REXT1): now also R110.2
- net at U1.E14 (REF_FILT1): now also C353.1
- net at U1.K23 (REF_REXT0): now also R111.2
- net at U1.K4 (REF_REXT2): now also R109.2
- net at U1.L23 (REF_FILT0): now also C354.1
- net at U1.L4 (REF_FILT2): now also C352.1
- net VSC_MDINT: now reaches U1.R2 (MDINT)
- new net CHGND: J18.SHLD, J19.SHLD, J20.SHLD, J21.SHLD, J4.SHLD, J8.SHLD
- new net PHY0_LED0_N: J4.31 (LED1_N), R81.1
- new net PHY0_LED1_N: J4.33 (LED2_G_N), R93.1
- new net PHY10_LED0_N: J21.31 (LED1_N), R91.1
- new net PHY10_LED1_N: J21.33 (LED2_G_N), R103.1
- new net PHY11_LED0_N: J21.27 (LED1_N), R92.1
- new net PHY11_LED1_N: J21.29 (LED2_G_N), R104.1
- new net PHY1_LED0_N: J4.27 (LED1_N), R82.1
- new net PHY1_LED1_N: J4.29 (LED2_G_N), R94.1
- new net PHY2_LED0_N: J8.31 (LED1_N), R83.1
- new net PHY2_LED1_N: J8.33 (LED2_G_N), R95.1
- new net PHY3_LED0_N: J8.27 (LED1_N), R84.1
- new net PHY3_LED1_N: J8.29 (LED2_G_N), R96.1
- new net PHY4_LED0_N: J18.31 (LED1_N), R85.1
- new net PHY4_LED1_N: J18.33 (LED2_G_N), R97.1
- new net PHY5_LED0_N: J18.27 (LED1_N), R86.1
- new net PHY5_LED1_N: J18.29 (LED2_G_N), R98.1
- new net PHY6_LED0_N: J19.31 (LED1_N), R87.1
- new net PHY6_LED1_N: J19.33 (LED2_G_N), R99.1
- new net PHY7_LED0_N: J19.27 (LED1_N), R88.1
- new net PHY7_LED1_N: J19.29 (LED2_G_N), R100.1
- new net PHY8_LED0_N: J20.31 (LED1_N), R89.1
- new net PHY8_LED1_N: J20.33 (LED2_G_N), R101.1
- new net PHY9_LED0_N: J20.27 (LED1_N), R90.1
- new net PHY9_LED1_N: J20.29 (LED2_G_N), R102.1
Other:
- note added: "Open drain"
- note added: "Strap: PHY addr MSBs = 2'b00"
- note added: "Strap: Refclk is 125 MHz"
- note added: "TODO: LVCMOS25 I/Os to FPGA Need level shifting"
- note added: "TODO: what is voltage range of refclk? is it internally terminated?"
- note added: "VSC8512 Hardware Design Checklist Section 8.2 page 23"
- moved on the sheet: U1A, U1E
